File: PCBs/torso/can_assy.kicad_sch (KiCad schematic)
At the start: 4 parts, among them U1 TJA1057GT/3J

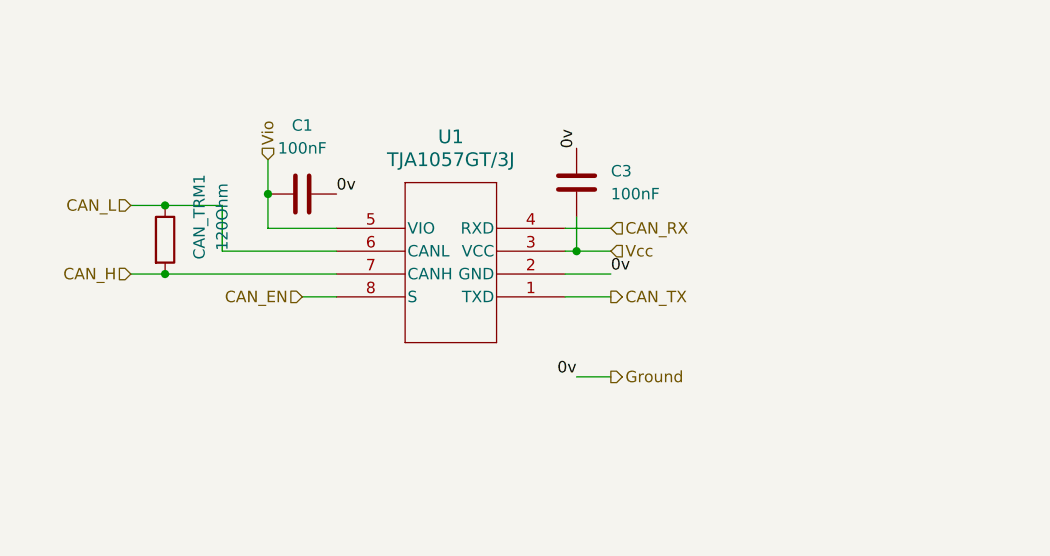
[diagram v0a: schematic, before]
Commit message: Torso all but complete, making bogie before checking the last mark
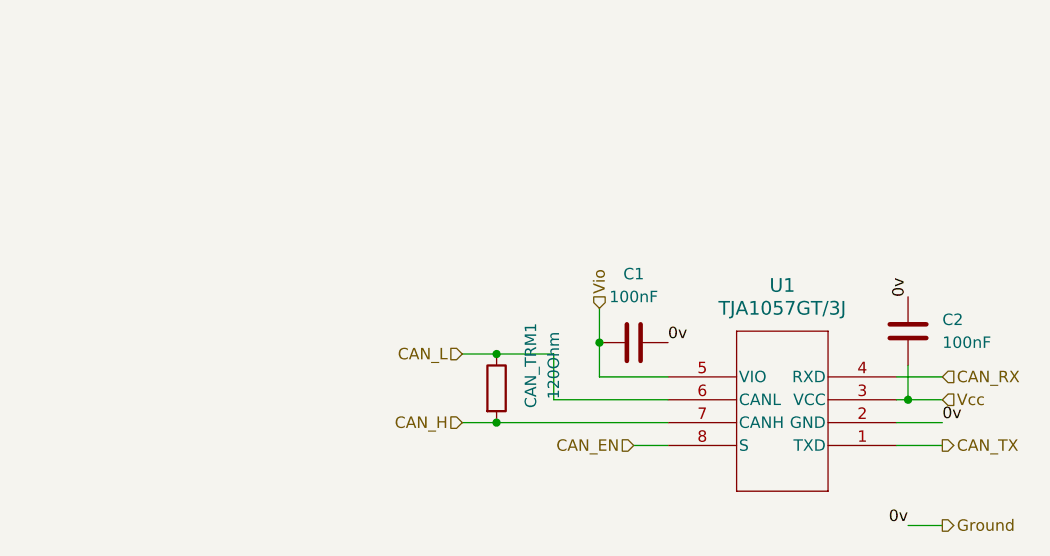
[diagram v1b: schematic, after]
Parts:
- removed C3: 100nF, Capacitor_SMD:C_0603_1608Metric, symbol Device:C
- added C2: 100nF, Capacitor_SMD:C_0603_1608Metric, symbol Device:C
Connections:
- net Ground: now also C2.2
- net Vcc: now also C2.1
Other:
- title: CAN assembly -> (none)

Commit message: merged changes from timertests, mostly documentation and such. Did not add tim6 config
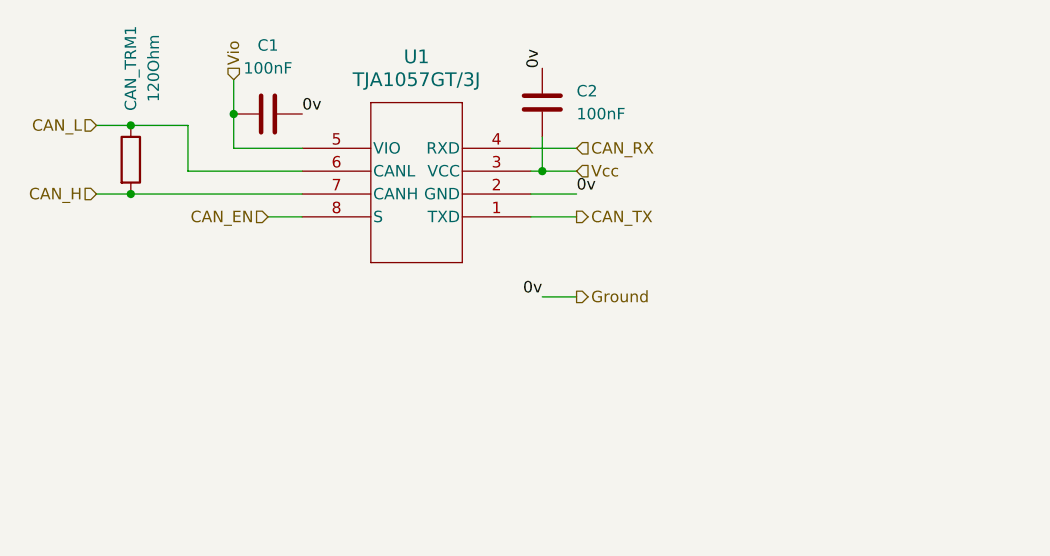
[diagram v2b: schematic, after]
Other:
- title: (none) -> CAN assembly
- moved on the sheet: C1, C2, CAN_TRM1, U1
